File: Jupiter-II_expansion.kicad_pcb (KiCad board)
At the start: 2 copper layers, 164.5 x 71.8 mm, 93 parts, among them J1 Conn_02x25_Odd_Even, J2 Conn_02x25_Odd_Even, J3 Conn_01x10, J4 Conn_01x03, J6 Conn_01x07, J7 Conn_02x15_Odd_Even, Q1 BC817, Q2 BC817, Q3 BC817, U1 GAL22V10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

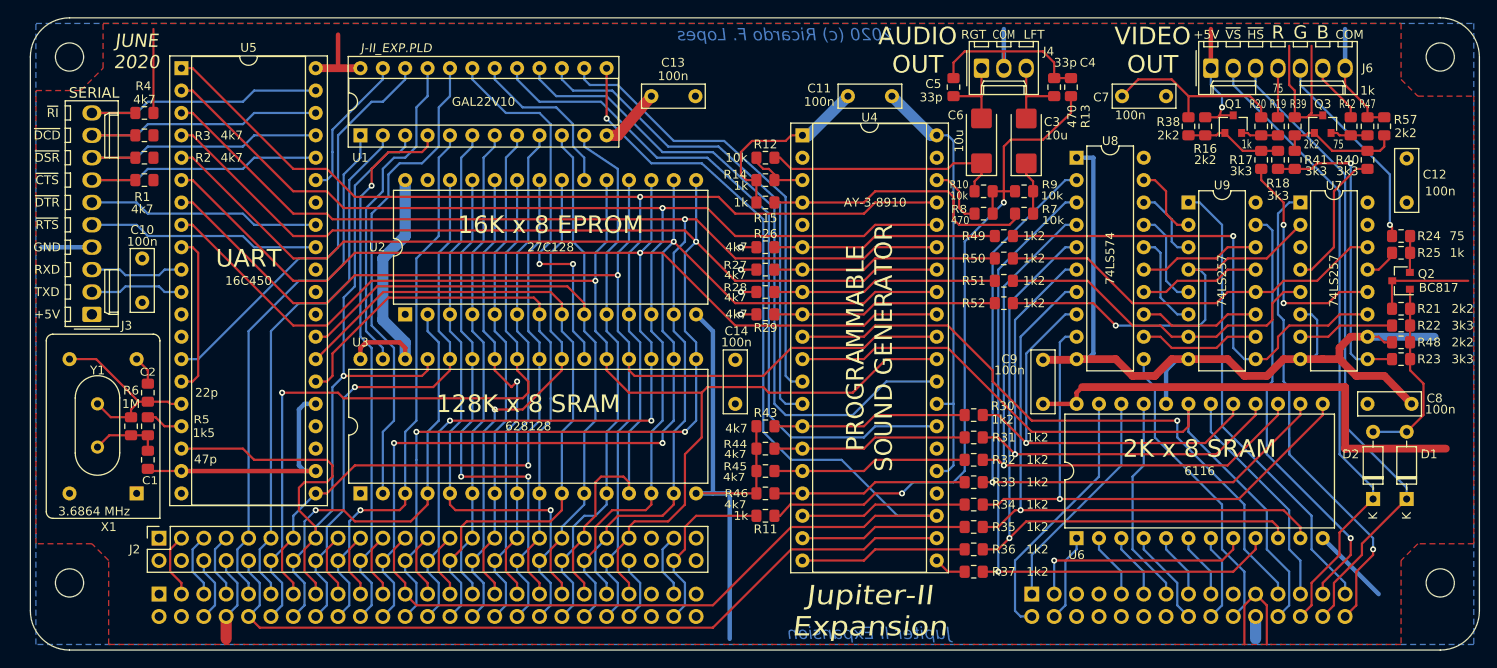
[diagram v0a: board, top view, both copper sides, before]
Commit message: First working version
Hardware validation
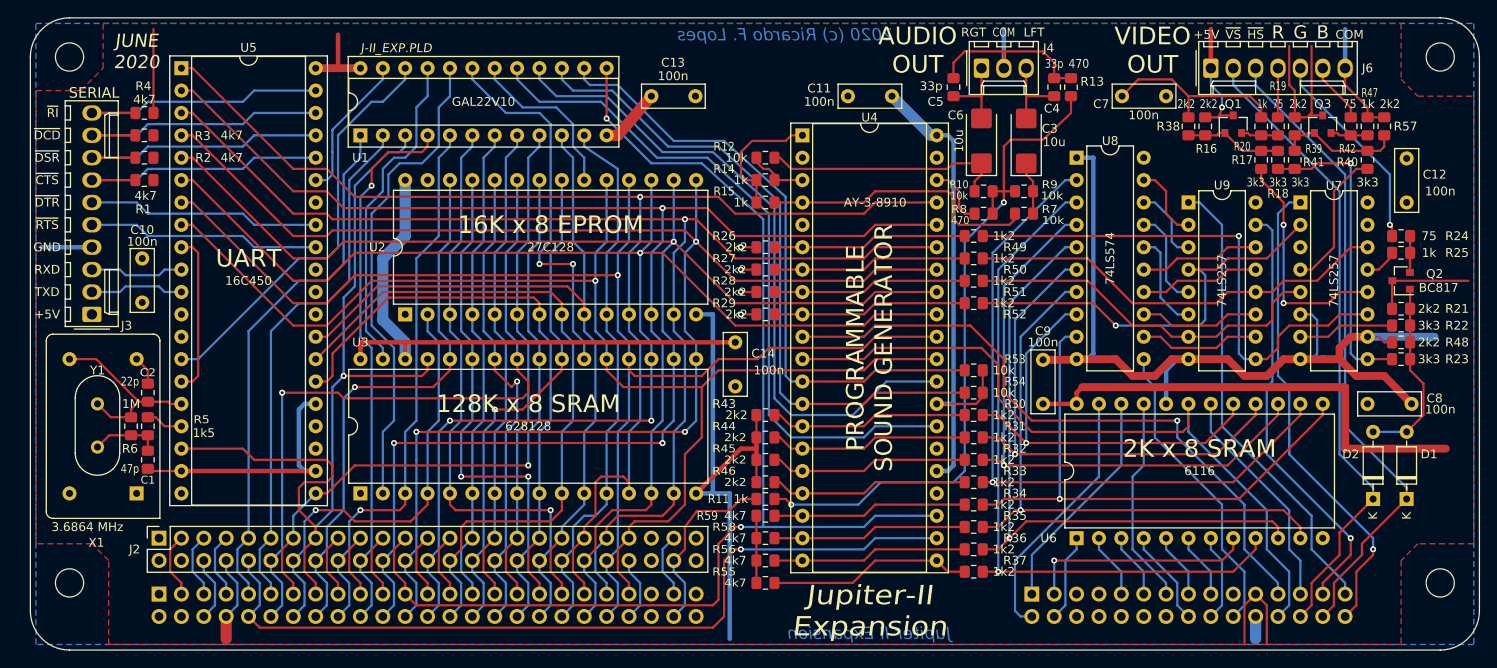
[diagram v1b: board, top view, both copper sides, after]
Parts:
- added R53: 10k, Resistor_SMD:R_0805_2012Metric_Pad1.15x1.40mm_HandSolder, F.Cu at (166.1, 102.9)
- added R54: 10k, Resistor_SMD:R_0805_2012Metric_Pad1.15x1.40mm_HandSolder, F.Cu at (166.1, 105.4)
- added R55: 4k7, Resistor_SMD:R_0805_2012Metric_Pad1.15x1.40mm_HandSolder, F.Cu at (142.5, 127.0)
- added R56: 4k7, Resistor_SMD:R_0805_2012Metric_Pad1.15x1.40mm_HandSolder, F.Cu at (142.5, 124.5)
- added R58: 4k7, Resistor_SMD:R_0805_2012Metric_Pad1.15x1.40mm_HandSolder, F.Cu at (142.5, 121.9)
- added R59: 4k7, Resistor_SMD:R_0805_2012Metric_Pad1.15x1.40mm_HandSolder, F.Cu at (142.5, 119.4)
- R26, R27, R28, R29, R43, R44, R45, R46: value 4k7 -> 2k2
- moved R49 3.42 mm to (166.1, 87.6)
- moved R50 3.42 mm to (166.1, 90.2)
- moved R51 3.42 mm to (166.1, 92.7)
- moved R52 3.42 mm to (166.1, 95.2)
- moved C14 1.99 mm to (139.1, 99.7)
- moved R11 1.91 mm to (142.5, 117.5)
- moved R44 1.27 mm to (142.5, 110.5)
- moved R46 1.27 mm to (142.5, 115.6)
- moved R43 1.27 mm to (142.5, 108.0)
- moved R45 1.27 mm to (142.5, 113.0)
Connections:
- net ~CPAGE renamed CPAGE
- net ~SPAGE renamed SPAGE
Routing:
- net +5V: track 220.7 -> 275.1 mm
- net INK_B: track 3.70 -> 23.2 mm
- net /XPAGE1: track 52.0 -> 70.9 mm
- net /XPAGE0: track 56.7 -> 75.2 mm
- net GNDD: track 308.9 -> 296.1 mm
- net /~RESET: track 148.3 -> 139.2 mm, vias 1 -> 2
- net Net-(R49-Pad2): track 56.3 -> 60.1 mm
- net /~CLK: track 90.2 -> 94.0 mm, vias 0 -> 1
- net BORDER_R: track 25.5 -> 22.1 mm
- net BORDER_I: track 25.5 -> 22.1 mm
- net BORDER_G: track 25.5 -> 22.1 mm
- net BORDER_B: track 25.5 -> 22.1 mm
- net Net-(R52-Pad2): track 45.2 -> 48.6 mm
- net Net-(R51-Pad2): track 38.5 -> 41.9 mm
- net Net-(R50-Pad2): track 45.0 -> 48.4 mm
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
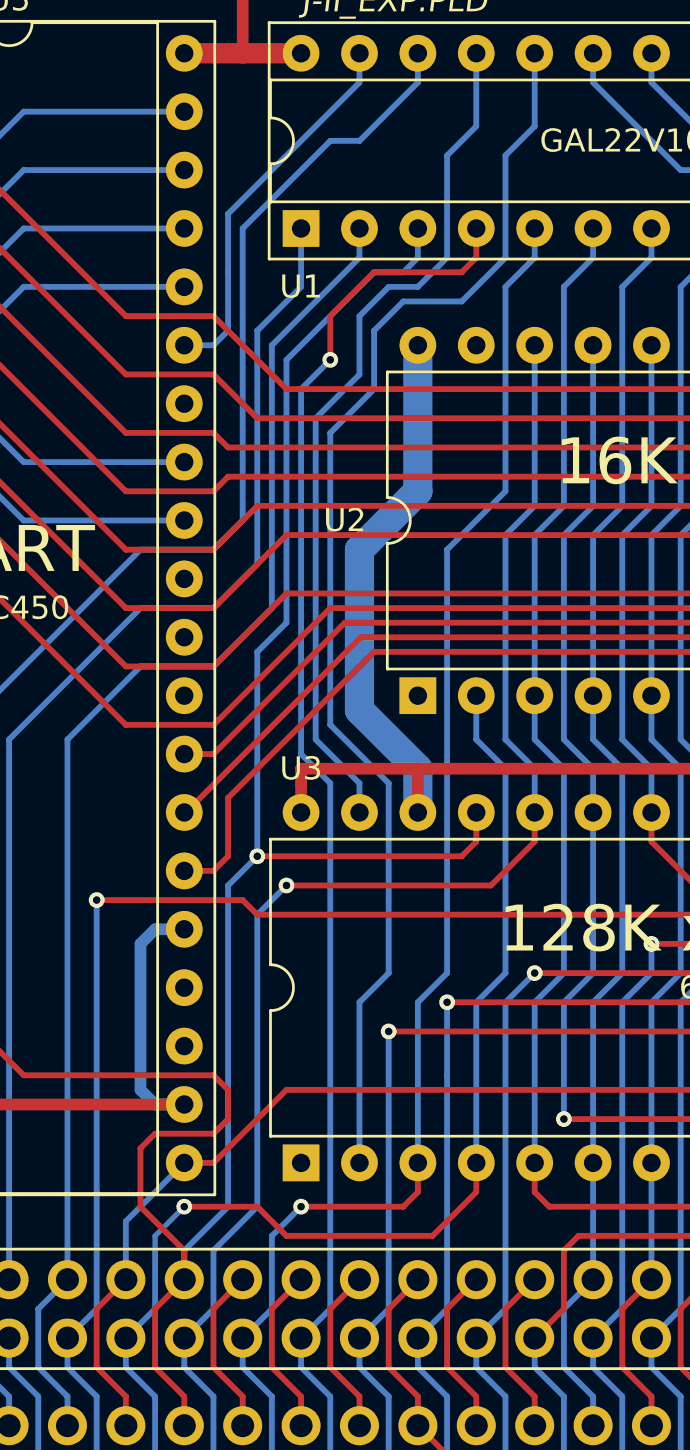
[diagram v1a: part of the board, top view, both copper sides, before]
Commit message: Corrected missing connections on XROM
Corrected missing connections on XROM pins 1 and 27
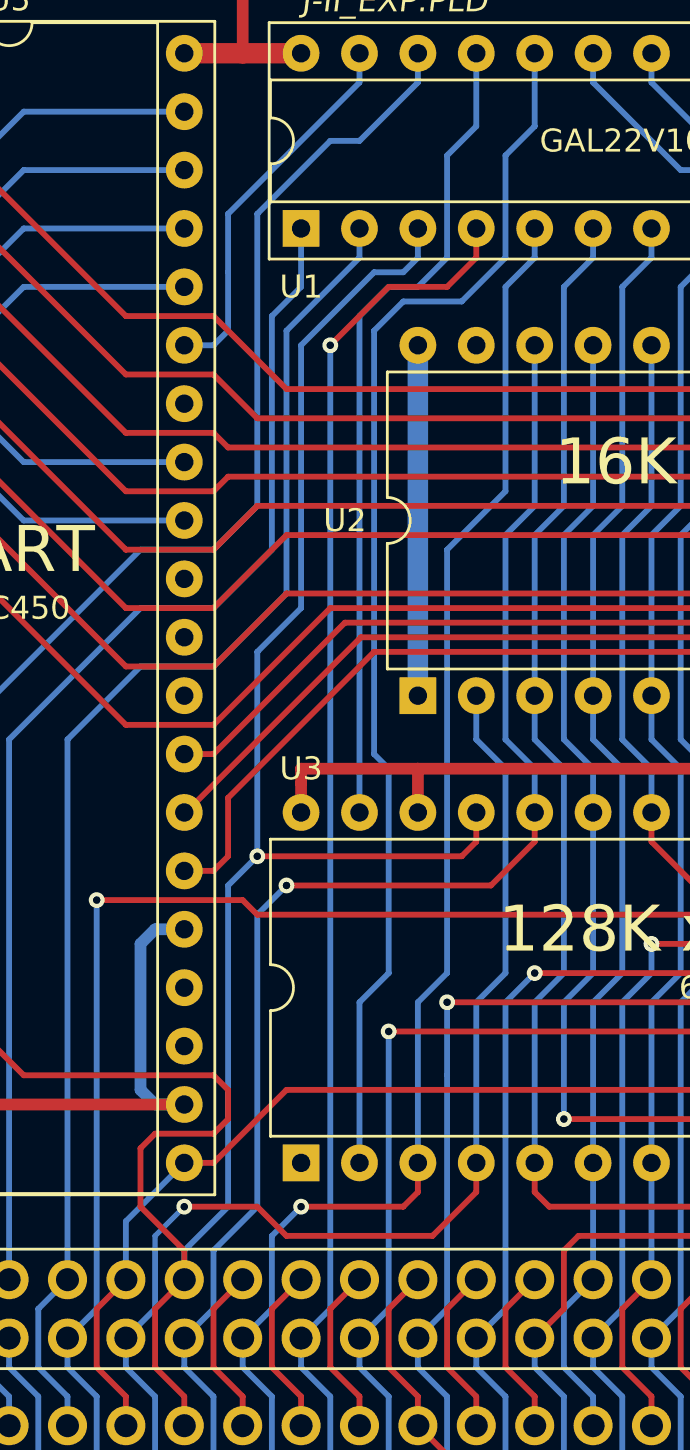
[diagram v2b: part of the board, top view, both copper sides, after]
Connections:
- U2 pad 1: Net-(U2-Pad1) -> +5V
- U2 pad 27: Net-(U2-Pad27) -> +5V
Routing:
- net +5V: track 275.1 -> 267.9 mm
- net A15: track 62.1 -> 60.3 mm
- net /XA15: track 38.1 -> 36.5 mm
- net /XA16: track 55.0 -> 53.4 mm
